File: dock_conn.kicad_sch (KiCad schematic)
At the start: 30 parts, among them J10 Conn_02x35_Odd_Even

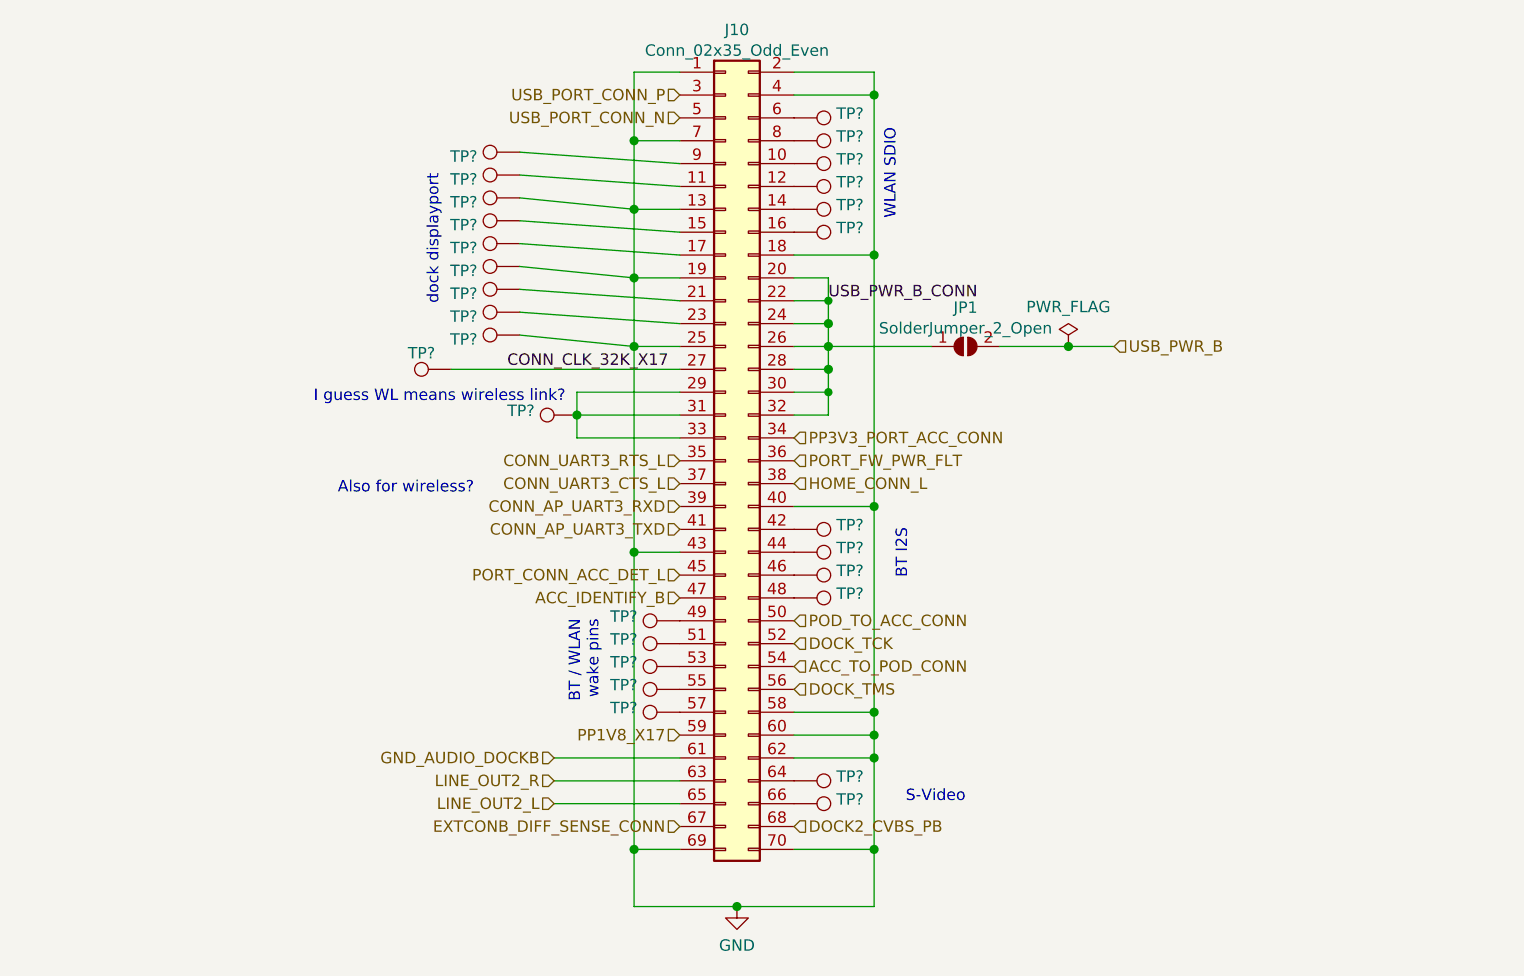
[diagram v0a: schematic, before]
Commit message: Flip J4 to back of board to reduce overall thickness in that area; re-route a whole bunch of signals to accomodate that.
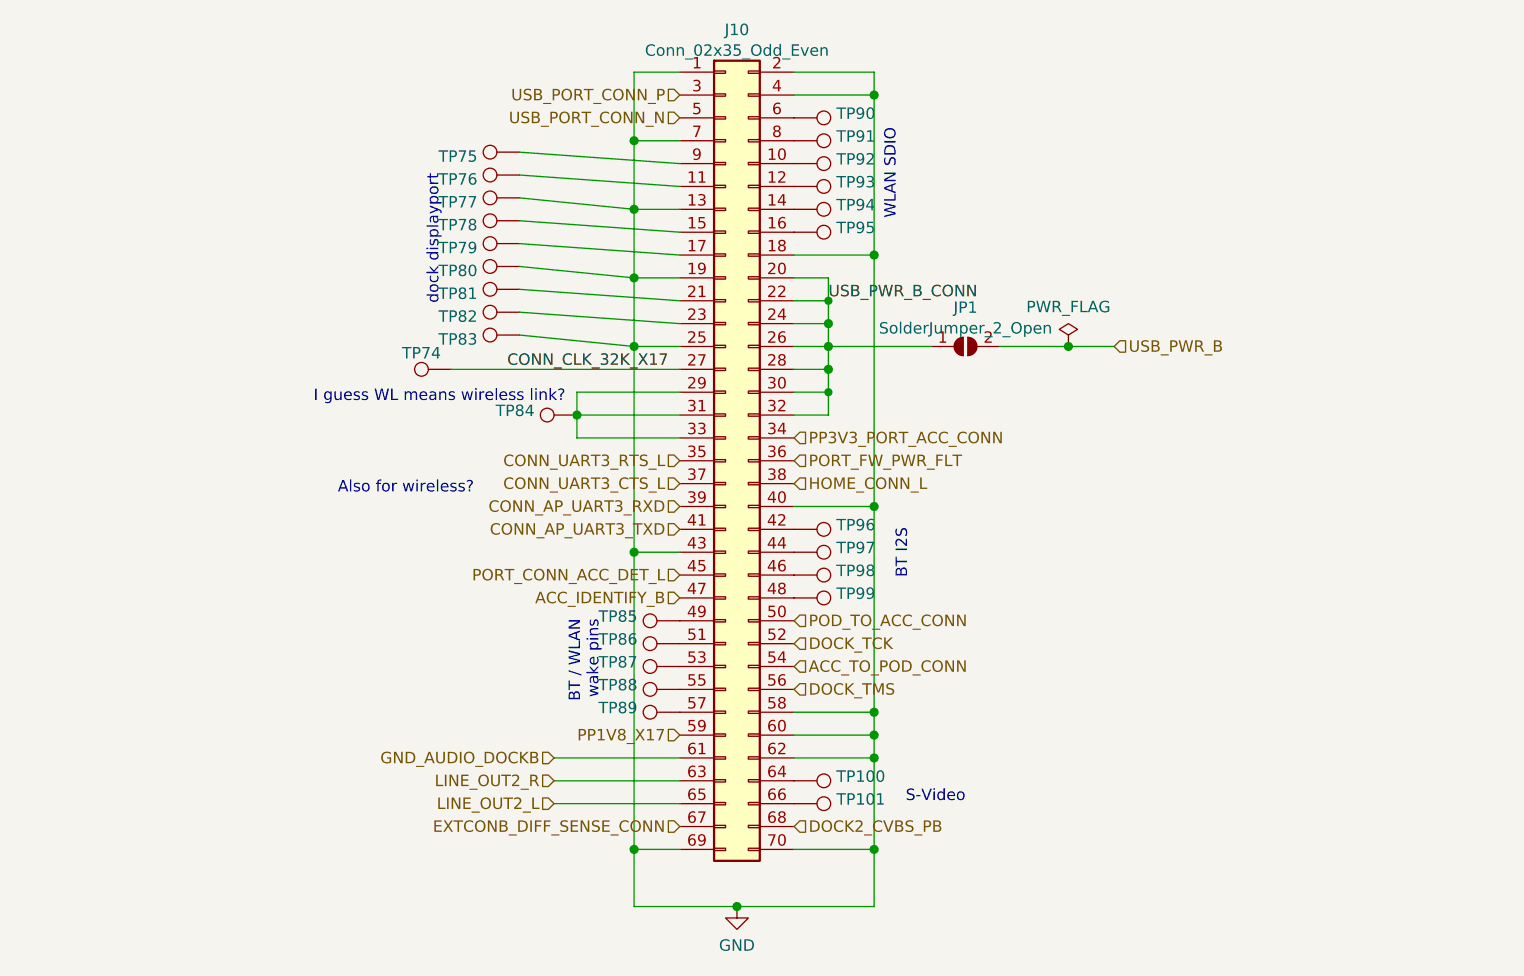
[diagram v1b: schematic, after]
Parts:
- gave numbers to parts that had none: 28
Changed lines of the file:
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@@
   (symbol (lib_id "Connector:TestPoint") (at 144.78 59.69 270) (mirror x) (unit 1)
     (in_bom yes) (on_board yes) (fields_autoplaced)
-    (property "Reference" "TP?" (id 0) (at 149.479 59.211 90)
+    (property "Reference" "TP93" (id 0) (at 149.479 59.211 90)
       (effects (font (size 1.27 1.27)) (justify left))
     )
@@
   (symbol (lib_id "Connector:TestPoint") (at 132.08 107.95 90) (unit 1)
     (in_bom yes) (on_board yes) (fields_autoplaced)
-    (property "Reference" "TP?" (id 0) (at 127.381 107.471 90)
+    (property "Reference" "TP85" (id 0) (at 127.381 107.471 90)
       (effects (font (size 1.27 1.27)) (justify left))
     )
@@
   (symbol (lib_id "Connector:TestPoint") (at 144.78 64.77 270) (mirror x) (unit 1)
     (in_bom yes) (on_board yes) (fields_autoplaced)
-    (property "Reference" "TP?" (id 0) (at 149.479 64.291 90)
+    (property "Reference" "TP95" (id 0) (at 149.479 64.291 90)
       (effects (font (size 1.27 1.27)) (justify left))
     )
@@
   (symbol (lib_id "Connector:TestPoint") (at 144.78 100.33 270) (mirror x) (unit 1)
     (in_bom yes) (on_board yes) (fields_autoplaced)
-    (property "Reference" "TP?" (id 0) (at 149.479 99.851 90)
+    (property "Reference" "TP97" (id 0) (at 149.479 99.851 90)
       (effects (font (size 1.27 1.27)) (justify left))
     )
@@
   (symbol (lib_id "Connector:TestPoint") (at 144.78 102.87 270) (mirror x) (unit 1)
     (in_bom yes) (on_board yes) (fields_autoplaced)
-    (property "Reference" "TP?" (id 0) (at 149.479 102.391 90)
+    (property "Reference" "TP98" (id 0) (at 149.479 102.391 90)
       (effects (font (size 1.27 1.27)) (justify left))
     )
@@
   (symbol (lib_id "Connector:TestPoint") (at 144.78 57.15 270) (mirror x) (unit 1)
     (in_bom yes) (on_board yes) (fields_autoplaced)
-    (property "Reference" "TP?" (id 0) (at 149.479 56.671 90)
+    (property "Reference" "TP92" (id 0) (at 149.479 56.671 90)
       (effects (font (size 1.27 1.27)) (justify left))
     )
@@
   (symbol (lib_id "Connector:TestPoint") (at 144.78 105.41 270) (mirror x) (unit 1)
     (in_bom yes) (on_board yes) (fields_autoplaced)
-    (property "Reference" "TP?" (id 0) (at 149.479 104.931 90)
+    (property "Reference" "TP99" (id 0) (at 149.479 104.931 90)
       (effects (font (size 1.27 1.27)) (justify left))
     )
@@
   (symbol (lib_id "Connector:TestPoint") (at 132.08 113.03 90) (unit 1)
     (in_bom yes) (on_board yes) (fields_autoplaced)
-    (property "Reference" "TP?" (id 0) (at 127.381 112.551 90)
+    (property "Reference" "TP87" (id 0) (at 127.381 112.551 90)
       (effects (font (size 1.27 1.27)) (justify left))
     )
@@
   (symbol (lib_id "Connector:TestPoint") (at 144.78 52.07 270) (mirror x) (unit 1)
     (in_bom yes) (on_board yes) (fields_autoplaced)
-    (property "Reference" "TP?" (id 0) (at 149.479 51.591 90)
+    (property "Reference" "TP90" (id 0) (at 149.479 51.591 90)
       (effects (font (size 1.27 1.27)) (justify left))
     )
@@
   (symbol (lib_id "Connector:TestPoint") (at 114.3 71.12 90) (mirror x) (unit 1)
     (in_bom yes) (on_board yes) (fields_autoplaced)
-    (property "Reference" "TP?" (id 0) (at 109.601 71.599 90)
+    (property "Reference" "TP81" (id 0) (at 109.601 71.599 90)
       (effects (font (size 1.27 1.27)) (justify left))
     )
@@
   (symbol (lib_id "Connector:TestPoint") (at 144.78 125.73 270) (mirror x) (unit 1)
     (in_bom yes) (on_board yes) (fields_autoplaced)
-    (property "Reference" "TP?" (id 0) (at 149.479 125.251 90)
+    (property "Reference" "TP100" (id 0) (at 149.479 125.251 90)
       (effects (font (size 1.27 1.27)) (justify left))
     )
@@
   (symbol (lib_id "Connector:TestPoint") (at 144.78 62.23 270) (mirror x) (unit 1)
     (in_bom yes) (on_board yes) (fields_autoplaced)
-    (property "Reference" "TP?" (id 0) (at 149.479 61.751 90)
+    (property "Reference" "TP94" (id 0) (at 149.479 61.751 90)
       (effects (font (size 1.27 1.27)) (justify left))
     )
@@
   (symbol (lib_id "Connector:TestPoint") (at 106.68 80.01 90) (mirror x) (unit 1)
     (in_bom yes) (on_board yes) (fields_autoplaced)
-    (property "Reference" "TP?" (id 0) (at 103.378 78.2122 90))
+    (property "Reference" "TP74" (id 0) (at 103.378 78.2122 90))
     (property "Value" "TestPoint" (id 1) (at 101.981 81.8766 90)
       (effects (font (size 1.27 1.27)) (justify left) hide)
@@
   (symbol (lib_id "Connector:TestPoint") (at 114.3 76.2 90) (mirror x) (unit 1)
     (in_bom yes) (on_board yes) (fields_autoplaced)
-    (property "Reference" "TP?" (id 0) (at 109.601 76.679 90)
+    (property "Reference" "TP83" (id 0) (at 109.601 76.679 90)
       (effects (font (size 1.27 1.27)) (justify left))
     )
@@
   (symbol (lib_id "Connector:TestPoint") (at 144.78 97.79 270) (mirror x) (unit 1)
     (in_bom yes) (on_board yes) (fields_autoplaced)
-    (property "Reference" "TP?" (id 0) (at 149.479 97.311 90)
+    (property "Reference" "TP96" (id 0) (at 149.479 97.311 90)
       (effects (font (size 1.27 1.27)) (justify left))
     )
@@
   (symbol (lib_id "Connector:TestPoint") (at 132.08 118.11 90) (unit 1)
     (in_bom yes) (on_board yes) (fields_autoplaced)
-    (property "Reference" "TP?" (id 0) (at 127.381 117.631 90)
+    (property "Reference" "TP89" (id 0) (at 127.381 117.631 90)
       (effects (font (size 1.27 1.27)) (justify left))
     )
@@
   (symbol (lib_id "Connector:TestPoint") (at 132.08 115.57 90) (unit 1)
     (in_bom yes) (on_board yes) (fields_autoplaced)
-    (property "Reference" "TP?" (id 0) (at 127.381 115.091 90)
+    (property "Reference" "TP88" (id 0) (at 127.381 115.091 90)
       (effects (font (size 1.27 1.27)) (justify left))
     )
@@
   (symbol (lib_id "Connector:TestPoint") (at 114.3 58.42 90) (mirror x) (unit 1)
     (in_bom yes) (on_board yes) (fields_autoplaced)
-    (property "Reference" "TP?" (id 0) (at 109.601 58.899 90)
+    (property "Reference" "TP76" (id 0) (at 109.601 58.899 90)
       (effects (font (size 1.27 1.27)) (justify left))
     )
@@
   (symbol (lib_id "Connector:TestPoint") (at 114.3 63.5 90) (mirror x) (unit 1)
     (in_bom yes) (on_board yes) (fields_autoplaced)
-    (property "Reference" "TP?" (id 0) (at 109.601 63.979 90)
+    (property "Reference" "TP78" (id 0) (at 109.601 63.979 90)
       (effects (font (size 1.27 1.27)) (justify left))
     )
@@
   (symbol (lib_id "Connector:TestPoint") (at 132.08 110.49 90) (unit 1)
     (in_bom yes) (on_board yes) (fields_autoplaced)
-    (property "Reference" "TP?" (id 0) (at 127.381 110.011 90)
+    (property "Reference" "TP86" (id 0) (at 127.381 110.011 90)
       (effects (font (size 1.27 1.27)) (justify left))
     )
@@
   (symbol (lib_id "Connector:TestPoint") (at 114.3 66.04 90) (mirror x) (unit 1)
     (in_bom yes) (on_board yes) (fields_autoplaced)
-    (property "Reference" "TP?" (id 0) (at 109.601 66.519 90)
+    (property "Reference" "TP79" (id 0) (at 109.601 66.519 90)
       (effects (font (size 1.27 1.27)) (justify left))
     )
@@
   (symbol (lib_id "Connector:TestPoint") (at 114.3 55.88 90) (mirror x) (unit 1)
     (in_bom yes) (on_board yes) (fields_autoplaced)
-    (property "Reference" "TP?" (id 0) (at 109.601 56.359 90)
+    (property "Reference" "TP75" (id 0) (at 109.601 56.359 90)
       (effects (font (size 1.27 1.27)) (justify left))
     )
@@
   (symbol (lib_id "Connector:TestPoint") (at 144.78 128.27 270) (mirror x) (unit 1)
     (in_bom yes) (on_board yes) (fields_autoplaced)
-    (property "Reference" "TP?" (id 0) (at 149.479 127.791 90)
+    (property "Reference" "TP101" (id 0) (at 149.479 127.791 90)
       (effects (font (size 1.27 1.27)) (justify left))
     )
@@
   (symbol (lib_id "Connector:TestPoint") (at 144.78 54.61 270) (mirror x) (unit 1)
     (in_bom yes) (on_board yes) (fields_autoplaced)
-    (property "Reference" "TP?" (id 0) (at 149.479 54.131 90)
+    (property "Reference" "TP91" (id 0) (at 149.479 54.131 90)
       (effects (font (size 1.27 1.27)) (justify left))
     )
@@
   (symbol (lib_id "Connector:TestPoint") (at 114.3 68.58 90) (mirror x) (unit 1)
     (in_bom yes) (on_board yes) (fields_autoplaced)
-    (property "Reference" "TP?" (id 0) (at 109.601 69.059 90)
+    (property "Reference" "TP80" (id 0) (at 109.601 69.059 90)
       (effects (font (size 1.27 1.27)) (justify left))
     )
@@
   (symbol (lib_id "Connector:TestPoint") (at 120.65 85.09 90) (unit 1)
     (in_bom yes) (on_board yes) (fields_autoplaced)
-    (property "Reference" "TP?" (id 0) (at 115.951 84.611 90)
+    (property "Reference" "TP84" (id 0) (at 115.951 84.611 90)
       (effects (font (size 1.27 1.27)) (justify left))
     )
@@
   (symbol (lib_id "Connector:TestPoint") (at 114.3 73.66 90) (mirror x) (unit 1)
     (in_bom yes) (on_board yes) (fields_autoplaced)
-    (property "Reference" "TP?" (id 0) (at 109.601 74.139 90)
+    (property "Reference" "TP82" (id 0) (at 109.601 74.139 90)
       (effects (font (size 1.27 1.27)) (justify left))
     )
@@
   (symbol (lib_id "Connector:TestPoint") (at 114.3 60.96 90) (mirror x) (unit 1)
     (in_bom yes) (on_board yes) (fields_autoplaced)
-    (property "Reference" "TP?" (id 0) (at 109.601 61.439 90)
-      (effects (font (size 1.27 1.27)) (justify left))
-    )
+    (property "Reference" "TP77" (id 0) (at 109.601 61.439 90)
+      (effects (font (size 1.27 1.27)) (justify left))
+    )

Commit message: Make footprint for the mounting holes, make them round instead of square. Also add an RTC.
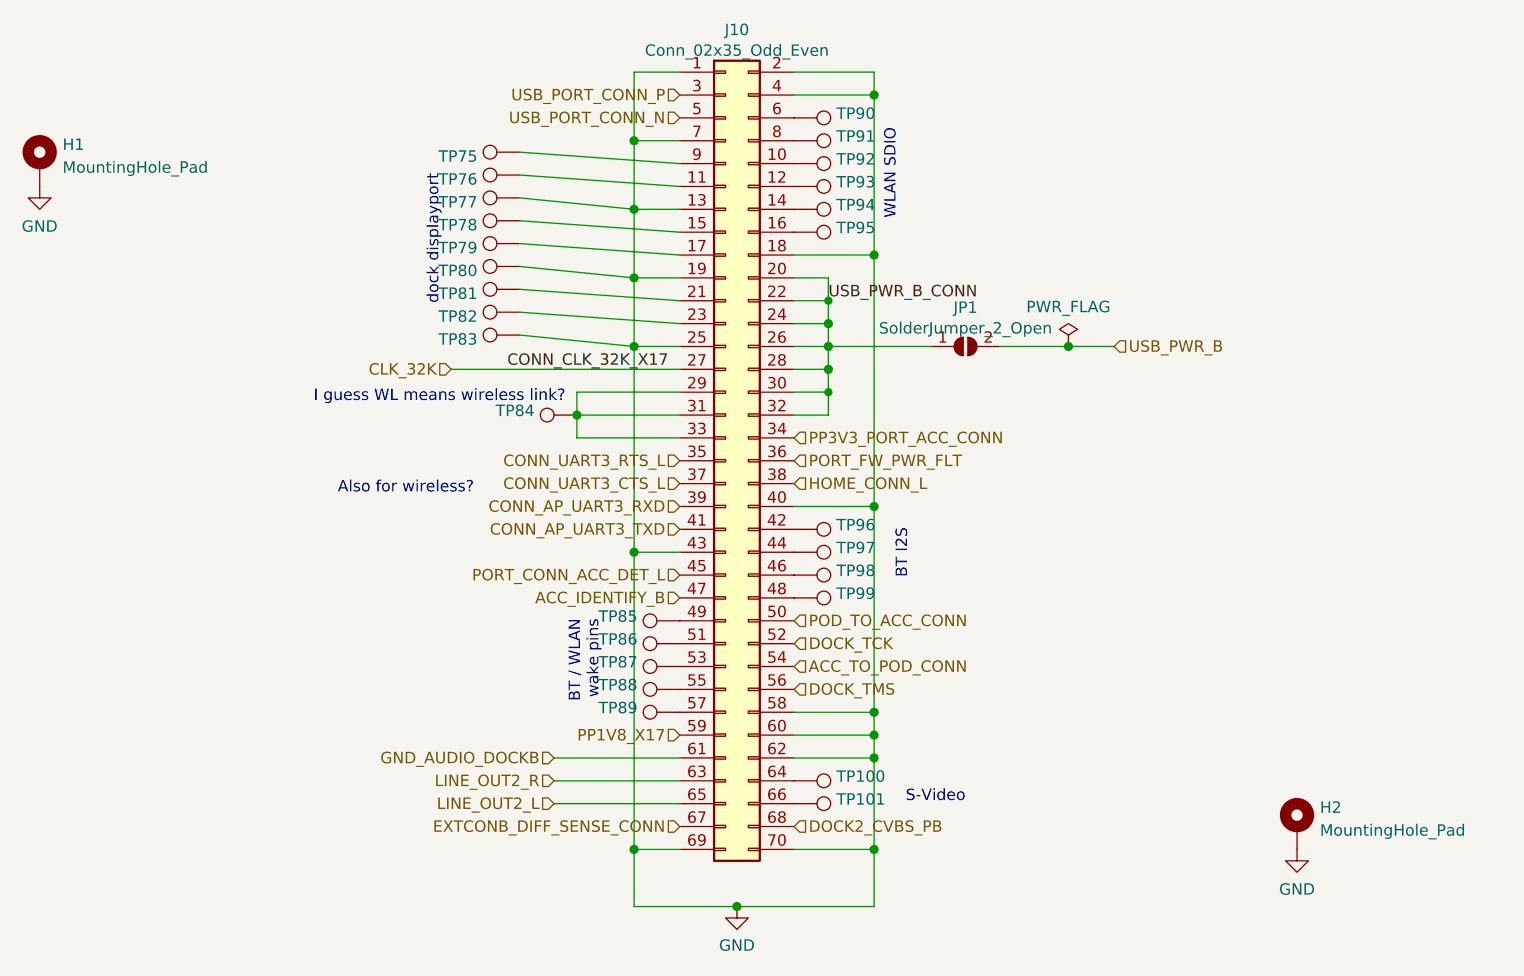
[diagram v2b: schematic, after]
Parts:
- removed TP74: TestPoint, footprints:testpoint_small, symbol Connector:TestPoint
- added H1, H2: MountingHole_Pad, footprints:MountHole_1.3mm_TopCopper, symbol Mechanical:MountingHole_Pad
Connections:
- net GND: now also H1.1, H2.1
- net CONN_CLK_32K_X17 renamed CLK_32K
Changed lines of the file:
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@@
+    (effects (font (size 1.27 1.27)) (justify right))
+  )
+  (hierarchical_label "CLK_32K" (shape input) (at 106.68 80.01 180)
     (effects (font (size 1.27 1.27)) (justify right))
   )
@@
     (effects (font (size 1.27 1.27)) (justify right))
   )
+  (symbol (lib_id "Mechanical:MountingHole_Pad") (at 60.96 57.15 0) (unit 1)
+    (in_bom yes) (on_board yes) (fields_autoplaced)
+    (property "Reference" "H1" (id 0) (at 63.5 55.0453 0)
+      (effects (font (size 1.27 1.27)) (justify left))
+    )
+    (property "Value" "MountingHole_Pad" (id 1) (at 63.5 57.5822 0)
+      (effects (font (size 1.27 1.27)) (justify left))
+    )
+    (property "Footprint" "footprints:MountHole_1.3mm_TopCopper" (id 2) (at 60.96 57.15 0)
+      (effects (font (size 1.27 1.27)) hide)
+    )
+    (property "Datasheet" "~" (id 3) (at 60.96 57.15 0)
+      (effects (font (size 1.27 1.27)) hide)
+    )
+    (pin "1")
+  )
   (symbol (lib_id "Connector:TestPoint") (at 144.78 59.69 270) (mirror x) (unit 1)
     (in_bom yes) (on_board yes) (fields_autoplaced)
@@
     )
     (property "Datasheet" "~" (id 3) (at 132.08 102.87 0)
+      (effects (font (size 1.27 1.27)) hide)
+    )
+    (pin "1")
+  )
+  (symbol (lib_id "Mechanical:MountingHole_Pad") (at 200.66 130.81 0) (unit 1)
+    (in_bom yes) (on_board yes) (fields_autoplaced)
+    (property "Reference" "H2" (id 0) (at 203.2 128.7053 0)
+      (effects (font (size 1.27 1.27)) (justify left))
+    )
+    (property "Value" "MountingHole_Pad" (id 1) (at 203.2 131.2422 0)
+      (effects (font (size 1.27 1.27)) (justify left))
+    )
+    (property "Footprint" "footprints:MountHole_1.3mm_TopCopper" (id 2) (at 200.66 130.81 0)
+      (effects (font (size 1.27 1.27)) hide)
+    )
+    (property "Datasheet" "~" (id 3) (at 200.66 130.81 0)
+      (effects (font (size 1.27 1.27)) hide)
+    )
+    (pin "1")
+  )
+  (symbol (lib_id "power:GND") (at 60.96 59.69 0) (unit 1)
+    (in_bom yes) (on_board yes) (fields_autoplaced)
+    (property "Reference" "#PWR048" (id 0) (at 60.96 66.04 0)
+      (effects (font (size 1.27 1.27)) hide)
+    )
+    (property "Value" "GND" (id 1) (at 60.96 64.1334 0))
+    (property "Footprint" "" (id 2) (at 60.96 59.69 0)
+      (effects (font (size 1.27 1.27)) hide)
+    )
+    (property "Datasheet" "" (id 3) (at 60.96 59.69 0)
       (effects (font (size 1.27 1.27)) hide)
     )
@@
     (pin "1")
   )
+  (symbol (lib_id "power:GND") (at 200.66 133.35 0) (unit 1)
+    (in_bom yes) (on_board yes) (fields_autoplaced)
+    (property "Reference" "#PWR049" (id 0) (at 200.66 139.7 0)
+      (effects (font (size 1.27 1.27)) hide)
+    )
+    (property "Value" "GND" (id 1) (at 200.66 137.7934 0))
+    (property "Footprint" "" (id 2) (at 200.66 133.35 0)
+      (effects (font (size 1.27 1.27)) hide)
+    )
+    (property "Datasheet" "" (id 3) (at 200.66 133.35 0)
+      (effects (font (size 1.27 1.27)) hide)
+    )
+    (pin "1")
+  )
   (symbol (lib_id "Connector:TestPoint") (at 144.78 62.23 270) (mirror x) (unit 1)
     (in_bom yes) (on_board yes) (fields_autoplaced)
@@
       (effects (font (size 1.27 1.27)) hide)
     )
-    (pin "1")
-  )
-  (symbol (lib_id "Connector:TestPoint") (at 106.68 80.01 90) (mirror x) (unit 1)
-    (in_bom yes) (on_board yes) (fields_autoplaced)
-    (property "Reference" "TP74" (id 0) (at 103.378 78.2122 90))
-    (property "Value" "TestPoint" (id 1) (at 101.981 81.8766 90)
-      (effects (font (size 1.27 1.27)) (justify left) hide)
-    )
-    (property "Footprint" "footprints:testpoint_small" (id 2) (at 106.68 85.09 0)
-      (effects (font (size 1.27 1.27)) hide)
-    )
-    (property "Datasheet" "~" (id 3) (at 106.68 85.09 0)
-      (effects (font (size 1.27 1.27)) hide)
-    )
